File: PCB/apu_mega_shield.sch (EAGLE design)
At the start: 36 parts, among them IC1 74HCT573D, IC2 4050D, IC3 DS1307, Q1 32.768, U1 IS62C1024AL-35QLI, X1 MICROSD

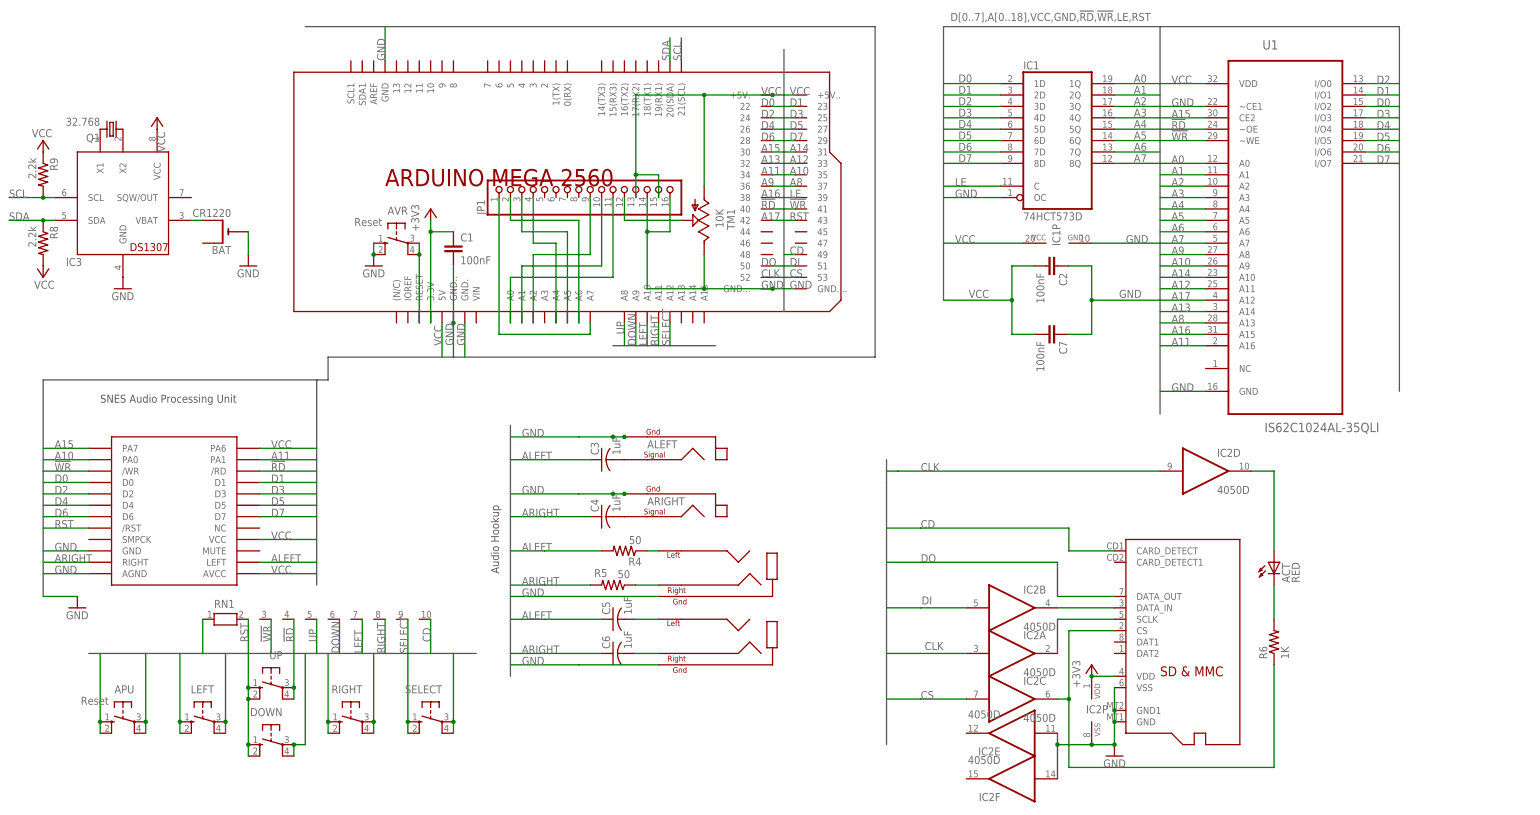
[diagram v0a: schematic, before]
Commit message: Added 3.3v regulator due to Arduino 3.3v line being limited to 50ma. (Micro SD cards can draw up to 100ma while they are being written to.)
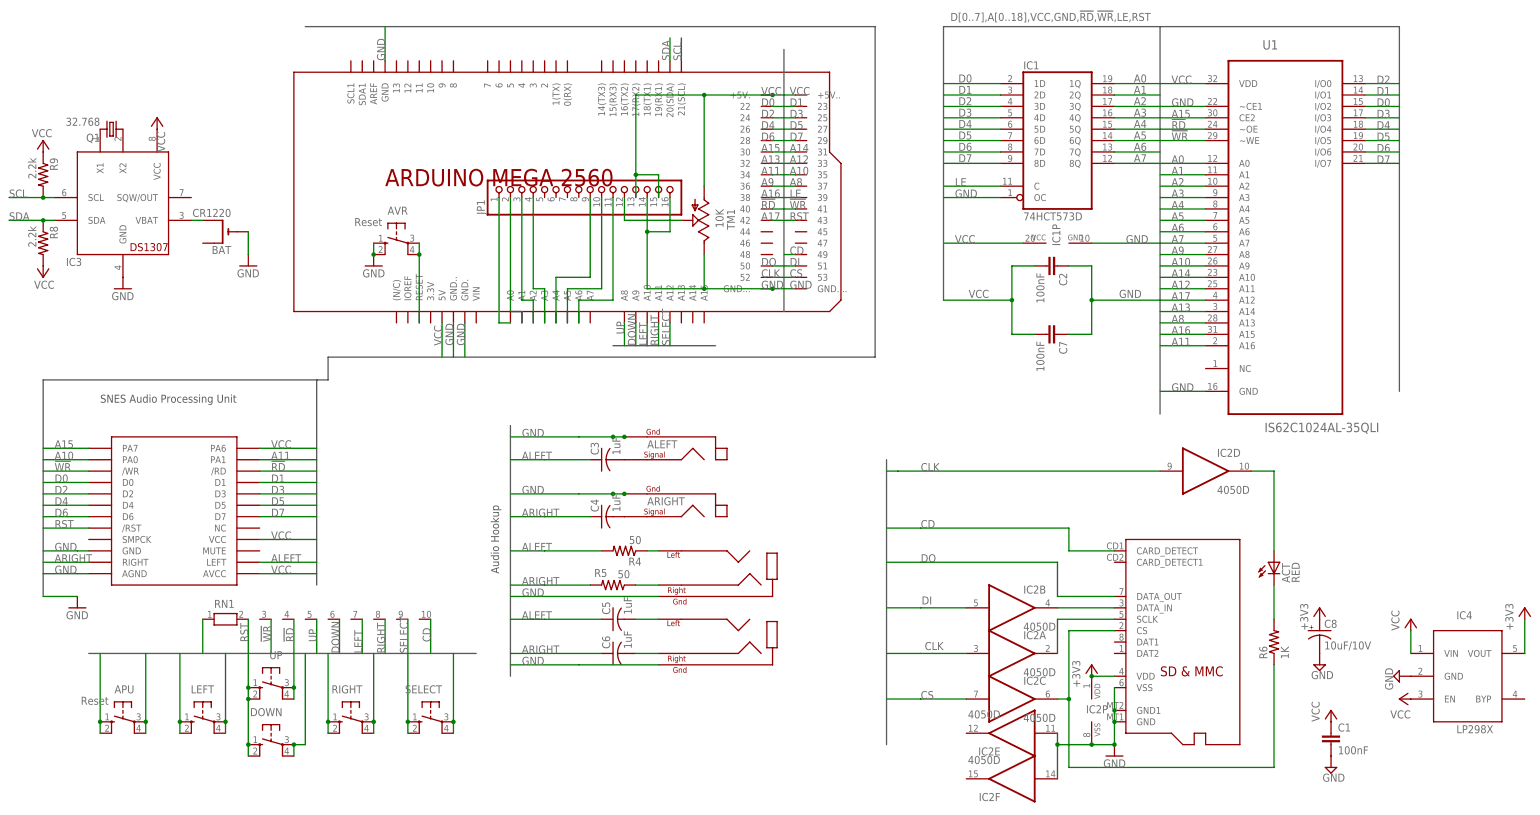
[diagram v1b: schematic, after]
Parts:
- added C8: 10uF/10V, adafruit:CPOL-USA/3216-18R
- added IC4: LP298XS, adafruit:LP298XS
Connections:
- removed net N$14: JP1.11, U$6.A0
- removed net N$15: JP1.10, U$6.A1
- removed net N$16: JP1.9, U$6.A2
- removed net N$17: JP1.4, U$6.A4
- removed net N$18: JP1.3, U$6.A5
- removed net N$19: JP1.2, U$6.A6
- removed net N$20: JP1.1, U$6.A7
- new net LCD_D4: JP1.4, U$6.A3
- new net LCD_D5: JP1.3, U$6.A2
- new net LCD_D6: JP1.2, U$6.A1
- new net LCD_D7: JP1.1, U$6.A0
- new net LCD_E: JP1.9, U$6.A4
- new net LCD_R!W: JP1.10, U$6.A5
- new net LCD_RS: JP1.11, U$6.A6
- net +3V3: now also C8.+, IC4.VOUT; no longer C1.1, U$6.3.3V
- net GND: now also C8.-, IC4.GND
- net VCC: now also C1.1, IC4.EN, IC4.VIN
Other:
- moved on the sheet: C1

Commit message: LCD now interfaced using 8-bit mode instead of 4-bit mode.
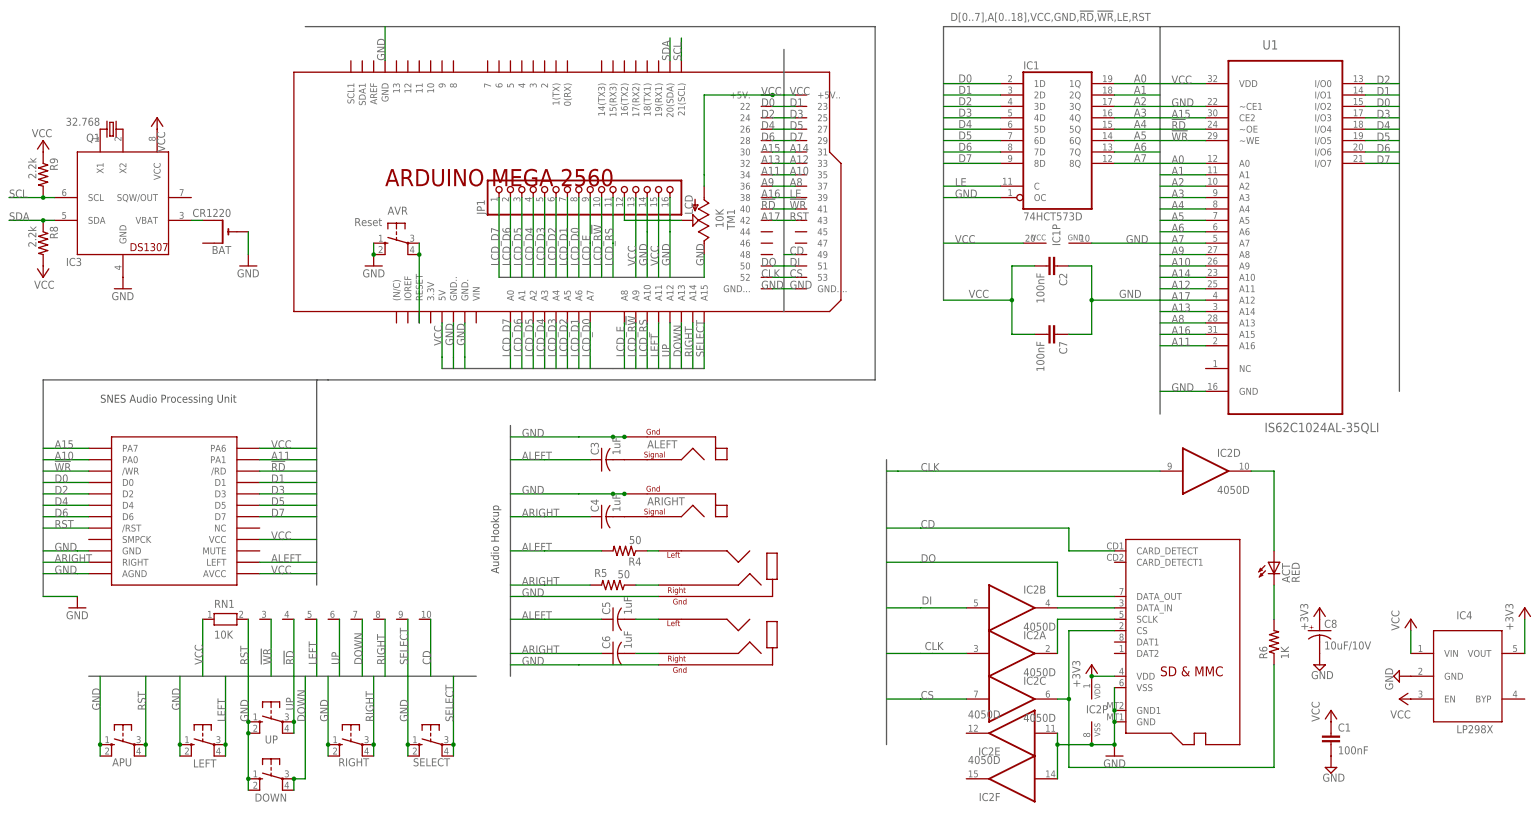
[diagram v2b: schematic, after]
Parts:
- JP1: value (none) -> LCD
- RN1: value (none) -> 10K
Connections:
- new net LCD_D0: JP1.8, U$6.A7
- new net LCD_D1: JP1.7, U$6.A6
- new net LCD_D2: JP1.6, U$6.A5
- new net LCD_D3: JP1.5, U$6.A4
- net DOWN: now also RN1.7, U$6.A13; no longer RN1.6, U$6.A9
- net LCD_E: now also U$6.A8; no longer U$6.A4
- net LCD_R!W: now also U$6.A9; no longer U$6.A5
- net LCD_RS: now also U$6.A10; no longer U$6.A6
- net LEFT: now also RN1.5, U$6.A11; no longer RN1.7, U$6.A10
- net RIGHT: now also U$6.A14; no longer U$6.A11
- net SELECT: now also U$6.A15; no longer U$6.A12
- net UP: now also RN1.6, U$6.A12; no longer RN1.5, U$6.A8
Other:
- moved on the sheet: APU, DOWN, LEFT, RIGHT, SELECT, UP

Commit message: Hopefully final PCB design for version 1.0 :)
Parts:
- added R1: 220, adafruit:R-US_0207/10
- IC1: value 74HCT573D -> 74AHC573
- U1: value IS62C1024AL-35QLI -> IS62C1024AL
- X1: value MICROSD -> MICROSDMOLEX; device adafruit:MICROSD -> adafruit:MICROSDMOLEX
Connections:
- new net N$14: JP1.15, R1.2
- net VCC: now also R1.1; no longer JP1.15
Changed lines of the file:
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@@
 <part name="C2" library="rcl" deviceset="C-EU" device="C0805" value="100nF"/>
 <part name="C7" library="rcl" deviceset="C-EU" device="C0805" value="100nF"/>
-<part name="IC1" library="74xx-eu" deviceset="74*573" device="D" technology="HCT"/>
-<part name="U1" library="ISSI_By_element14_Batch_1" deviceset="IS62C1024AL-35QLI" device=""/>
+<part name="IC1" library="74xx-eu" deviceset="74*573" device="D" technology="HCT" value="74AHC573"/>
+<part name="U1" library="ISSI_By_element14_Batch_1" deviceset="IS62C1024AL-35QLI" device="" value="IS62C1024AL"/>
 <part name="IC2" library="40xx" deviceset="4050" device="D"/>
-<part name="X1" library="adafruit" deviceset="MICROSD" device=""/>
 <part name="+3V2" library="supply1" deviceset="+3V3" device=""/>
 <part name="ACT" library="adafruit" deviceset="LED" device="CHIP-LED0805" value="RED"/>
@@
 <part name="P+1" library="supply1" deviceset="VCC" device=""/>
 <part name="SUPPLY2" library="supply2" deviceset="GND" device=""/>
+<part name="X1" library="adafruit" deviceset="MICROSD" device="MOLEX"/>
+<part name="R1" library="adafruit" deviceset="R-US_" device="0207/10" value="220"/>
 </parts>
 <sheets>
@@
 <instance part="IC2" gate="C" x="312.42" y="0"/>
 <instance part="IC2" gate="D" x="355.6" y="50.8"/>
-<instance part="X1" gate="G$1" x="353.06" y="15.24"/>
 <instance part="+3V2" gate="G$1" x="330.2" y="7.62"/>
 <instance part="ACT" gate="G$1" x="370.84" y="30.48"/>
@@
 <instance part="P+1" gate="VCC" x="383.54" y="-2.54"/>
 <instance part="SUPPLY2" gate="GND" x="383.54" y="-15.24"/>
+<instance part="X1" gate="G$1" x="353.06" y="15.24"/>
+<instance part="R1" gate="G$1" x="233.68" y="121.92" rot="R270"/>
 </instances>
 <busses>
@@
 <junction x="335.28" y="-2.54"/>
 <junction x="335.28" y="-5.08"/>
-<pinref part="X1" gate="G$1" pin="VSS"/>
-<pinref part="X1" gate="G$1" pin="GND1"/>
-<pinref part="X1" gate="G$1" pin="GND"/>
 <pinref part="GND1" gate="1" pin="GND"/>
 <pinref part="IC2" gate="P" pin="VSS"/>
@@
 <wire x1="322.58" y1="-10.16" x2="322.58" y2="-17.78" width="0.1524" layer="91"/>
 <junction x="322.58" y="-10.16"/>
+<pinref part="X1" gate="G$1" pin="GND"/>
+<pinref part="X1" gate="G$1" pin="GND1"/>
+<pinref part="X1" gate="G$1" pin="VSS"/>
 </segment>
 <segment>
@@
 <junction x="259.08" y="134.62"/>
 <wire x1="243.84" y1="134.62" x2="259.08" y2="134.62" width="0.1524" layer="91"/>
-<wire x1="243.84" y1="116.84" x2="243.84" y2="134.62" width="0.1524" layer="91"/>
+<wire x1="243.84" y1="116.84" x2="243.84" y2="127" width="0.1524" layer="91"/>
 <pinref part="TM1" gate="1" pin="A"/>
+<wire x1="243.84" y1="127" x2="243.84" y2="134.62" width="0.1524" layer="91"/>
 <wire x1="243.84" y1="114.3" x2="243.84" y2="116.84" width="0.1524" layer="91"/>
 <label x="256.54" y="134.62" size="1.778" layer="95"/>
+<pinref part="R1" gate="G$1" pin="1"/>
+<wire x1="233.68" y1="127" x2="243.84" y2="127" width="0.1524" layer="91"/>
+<junction x="243.84" y="127"/>
 </segment>
 <segment>
@@
 <wire x1="228.6" y1="111.76" x2="228.6" y2="93.98" width="0.1524" layer="91"/>
 <label x="228.6" y="96.52" size="1.778" layer="95" rot="R90"/>
-</segment>
-<segment>
-<pinref part="JP1" gate="A" pin="15"/>
-<wire x1="233.68" y1="111.76" x2="233.68" y2="93.98" width="0.1524" layer="91"/>
-<label x="233.68" y="96.52" size="1.778" layer="95" rot="R90"/>
 </segment>
 <segment>
@@
 <junction x="325.12" y="0"/>
 <pinref part="IC2" gate="C" pin="O"/>
+<pinref part="R6" gate="G$1" pin="1"/>
 <pinref part="X1" gate="G$1" pin="CS"/>
-<pinref part="R6" gate="G$1" pin="1"/>
 </segment>
 </net>
@@
 <segment>
 <wire x1="330.2" y1="5.08" x2="335.28" y2="5.08" width="0.1524" layer="91"/>
-<pinref part="X1" gate="G$1" pin="VDD"/>
 <pinref part="+3V2" gate="G$1" pin="+3V3"/>
 <pinref part="IC2" gate="P" pin="VDD"/>
 <junction x="330.2" y="5.08"/>
+<pinref part="X1" gate="G$1" pin="VDD"/>
 </segment>
 <segment>
@@
 <wire x1="325.12" y1="38.1" x2="292.1" y2="38.1" width="0.1524" layer="91"/>
 <label x="292.1" y="38.1" size="1.778" layer="95"/>
+<wire x1="292.1" y1="38.1" x2="284.48" y2="38.1" width="0.1524" layer="91"/>
 <pinref part="X1" gate="G$1" pin="CARD_DETECT"/>
-<wire x1="292.1" y1="38.1" x2="284.48" y2="38.1" width="0.1524" layer="91"/>
 </segment>
 <segment>
@@
 <wire x1="292.1" y1="30.48" x2="322.58" y2="30.48" width="0.1524" layer="91"/>
 <label x="292.1" y="30.48" size="1.778" layer="95"/>
+<wire x1="292.1" y1="30.48" x2="284.48" y2="30.48" width="0.1524" layer="91"/>
 <pinref part="X1" gate="G$1" pin="DATA_OUT"/>
-<wire x1="292.1" y1="30.48" x2="284.48" y2="30.48" width="0.1524" layer="91"/>
 </segment>
 <segment>
@@
 <segment>
 <wire x1="322.58" y1="20.32" x2="335.28" y2="20.32" width="0.1524" layer="91"/>
+<pinref part="IC2" gate="B" pin="O"/>
 <pinref part="X1" gate="G$1" pin="DATA_IN"/>
-<pinref part="IC2" gate="B" pin="O"/>
 </segment>
 </net>
@@
 </segment>
 </net>
+<net name="N$14" class="0">
+<segment>
+<pinref part="JP1" gate="A" pin="15"/>
+<pinref part="R1" gate="G$1" pin="2"/>
+<wire x1="233.68" y1="111.76" x2="233.68" y2="116.84" width="0.1524" layer="91"/>
+</segment>
+</net>
